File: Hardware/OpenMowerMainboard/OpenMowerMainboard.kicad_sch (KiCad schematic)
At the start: 26 parts

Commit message: Fuse holders and aternative led led pn from lcsc added
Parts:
- D23: LCSC (none) -> C84257
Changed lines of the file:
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@@
+      (effects (font (size 1.27 1.27)) hide)
+    )
+    (property "LCSC" "C84257" (id 7) (at 325.755 201.295 0)
       (effects (font (size 1.27 1.27)) hide)
     )

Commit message: BOM changes
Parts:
- FID1, FID10, FID11, FID12, FID13, FID14, FID15, FID16, FID2, FID3, FID4, FID5, FID6, FID7, FID8, FID9, H1, H2, H3, H4: DNP (none) -> Y
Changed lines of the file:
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@@
+      (effects (font (size 1.27 1.27)) hide)
+    )
+    (property "DNP" "Y" (id 5) (at 373.38 240.03 0)
       (effects (font (size 1.27 1.27)) hide)
     )
@@
       (effects (font (size 1.27 1.27)) hide)
     )
+    (property "DNP" "Y" (id 5) (at 378.46 240.03 0)
+      (effects (font (size 1.27 1.27)) hide)
+    )
     (pin "1")
   )
@@
       (effects (font (size 1.27 1.27)) hide)
     )
+    (property "DNP" "Y" (id 5) (at 383.54 240.03 0)
+      (effects (font (size 1.27 1.27)) hide)
+    )
     (pin "1")
   )
@@
       (effects (font (size 1.27 1.27)) hide)
     )
+    (property "DNP" "Y" (id 5) (at 388.62 240.03 0)
+      (effects (font (size 1.27 1.27)) hide)
+    )
     (pin "1")
   )
@@
       (effects (font (size 1.27 1.27)) hide)
     )
+    (property "DNP" "Y" (id 5) (at 380.365 38.735 0)
+      (effects (font (size 1.27 1.27)) hide)
+    )
   )
   (symbol (lib_id "Mechanical:Fiducial") (at 380.365 52.07 0) (unit 1)
@@
     )
     (property "Config" "do not place" (id 4) (at 380.365 52.07 0)
+      (effects (font (size 1.27 1.27)) hide)
+    )
+    (property "DNP" "Y" (id 5) (at 380.365 52.07 0)
       (effects (font (size 1.27 1.27)) hide)
     )
@@
       (effects (font (size 1.27 1.27)) hide)
     )
+    (property "DNP" "Y" (id 5) (at 380.365 25.4 0)
+      (effects (font (size 1.27 1.27)) hide)
+    )
   )
   (symbol (lib_id "Mechanical:Fiducial") (at 368.3 43.18 0) (unit 1)
@@
       (effects (font (size 1.27 1.27)) hide)
     )
+    (property "DNP" "Y" (id 5) (at 368.3 43.18 0)
+      (effects (font (size 1.27 1.27)) hide)
+    )
   )
   (symbol (lib_id "Mechanical:Fiducial") (at 368.3 47.625 0) (unit 1)
@@
     )
     (property "Config" "do not place" (id 4) (at 368.3 47.625 0)
+      (effects (font (size 1.27 1.27)) hide)
+    )
+    (property "DNP" "Y" (id 5) (at 368.3 47.625 0)
       (effects (font (size 1.27 1.27)) hide)
     )
@@
       (effects (font (size 1.27 1.27)) hide)
     )
+    (property "DNP" "Y" (id 5) (at 380.365 29.845 0)
+      (effects (font (size 1.27 1.27)) hide)
+    )
   )
   (symbol (lib_id "Device:LED") (at 325.755 201.295 90) (unit 1)
@@
     )
     (property "Config" "do not place" (id 4) (at 368.3 25.4 0)
+      (effects (font (size 1.27 1.27)) hide)
+    )
+    (property "DNP" "Y" (id 5) (at 368.3 25.4 0)
       (effects (font (size 1.27 1.27)) hide)
     )
@@
       (effects (font (size 1.27 1.27)) hide)
     )
+    (property "DNP" "Y" (id 5) (at 368.3 56.515 0)
+      (effects (font (size 1.27 1.27)) hide)
+    )
   )
   (symbol (lib_id "power:GND") (at 76.835 88.9 90) (unit 1)
@@
       (effects (font (size 1.27 1.27)) hide)
     )
+    (property "DNP" "Y" (id 5) (at 368.3 38.735 0)
+      (effects (font (size 1.27 1.27)) hide)
+    )
   )
   (symbol (lib_id "Device:R") (at 95.25 156.845 180) (unit 1)
@@
       (effects (font (size 1.27 1.27)) hide)
     )
+    (property "DNP" "Y" (id 5) (at 368.3 52.07 0)
+      (effects (font (size 1.27 1.27)) hide)
+    )
   )
   (symbol (lib_id "power:+5V") (at 325.755 193.04 0) (unit 1)
@@
       (effects (font (size 1.27 1.27)) hide)
     )
+    (property "DNP" "Y" (id 5) (at 380.365 34.29 0)
+      (effects (font (size 1.27 1.27)) hide)
+    )
   )
   (symbol (lib_id "Mechanical:Fiducial") (at 380.365 43.18 0) (unit 1)
@@
       (effects (font (size 1.27 1.27)) hide)
     )
+    (property "DNP" "Y" (id 5) (at 380.365 43.18 0)
+      (effects (font (size 1.27 1.27)) hide)
+    )
   )
   (symbol (lib_id "Mechanical:Fiducial") (at 380.365 47.625 0) (unit 1)
@@
     )
     (property "Config" "do not place" (id 4) (at 380.365 47.625 0)
+      (effects (font (size 1.27 1.27)) hide)
+    )
+    (property "DNP" "Y" (id 5) (at 380.365 47.625 0)
       (effects (font (size 1.27 1.27)) hide)
     )
@@
     )
     (property "Config" "do not place" (id 4) (at 368.3 29.845 0)
+      (effects (font (size 1.27 1.27)) hide)
+    )
+    (property "DNP" "Y" (id 5) (at 368.3 29.845 0)
       (effects (font (size 1.27 1.27)) hide)
     )
@@
       (effects (font (size 1.27 1.27)) hide)
     )
+    (property "DNP" "Y" (id 5) (at 380.365 56.515 0)
+      (effects (font (size 1.27 1.27)) hide)
+    )
   )
   (symbol (lib_id "Device:R") (at 325.755 210.185 180) (unit 1)
@@
     )
     (property "Config" "do not place" (id 4) (at 368.3 34.29 0)
+      (effects (font (size 1.27 1.27)) hide)
+    )
+    (property "DNP" "Y" (id 5) (at 368.3 34.29 0)
       (effects (font (size 1.27 1.27)) hide)
     )
@@
     )
     (path "/ea926745-863d-461e-9df3-dbf32112727b/1dbfe119-2837-4ceb-9076-5a2712ad0b2e"
-      (reference "C9") (unit 1) (value "DNP") (footprint "Capacitor_SMD:CP_Elec_10x12.5")
+      (reference "C9") (unit 1) (value "680uF") (footprint "Capacitor_SMD:CP_Elec_10x12.5")
     )
     (path "/ea926745-863d-461e-9df3-dbf32112727b/28797dd3-5c25-40ea-9029-91b4bdf67bc8"
-      (reference "C10") (unit 1) (value "680uF") (footprint "Capacitor_SMD:CP_Elec_10x12.5")
+      (reference "C10") (unit 1) (value "DNP") (footprint "Capacitor_SMD:CP_Elec_10x12.5")
     )
     (path "/ea926745-863d-461e-9df3-dbf32112727b/254c5ed7-6a5e-462f-bb7e-ae89a4710395"
@@
     )
     (path "/ea926745-863d-461e-9df3-dbf32112727b/5017618a-3028-4818-b382-40d730510d49"
-      (reference "C23") (unit 1) (value "DNP") (footprint "Capacitor_SMD:CP_Elec_10x12.5")
+      (reference "C23") (unit 1) (value "680uF") (footprint "Capacitor_SMD:CP_Elec_10x12.5")
     )
     (path "/c4934db8-1638-4ac4-bd06-84d03b3fc106/2884b602-ea4b-4182-a4ff-ddb6a99ed5db"
@@
       (reference "JP6") (unit 1) (value "SolderJumper_2_Bridged") (footprint "Jumper:SolderJumper-2_P1.3mm_Bridged_RoundedPad1.0x1.5mm")
     )
+    (path "/00000000-0000-0000-0000-000061080954/86e7b903-a105-407a-b12f-ed15cd7fb4ed"
+      (reference "JP7") (unit 1) (value "SolderJumper_2_Bridged") (footprint "Jumper:SolderJumper-2_P1.3mm_Bridged_RoundedPad1.0x1.5mm")
+    )
+    (path "/00000000-0000-0000-0000-000061080954/4ed5a4cb-42d2-4cd1-a2f4-be7f70116c48"
+      (reference "JP8") (unit 1) (value "SolderJumper_2_Bridged") (footprint "Jumper:SolderJumper-2_P1.3mm_Bridged_RoundedPad1.0x1.5mm")
+    )
     (path "/ea926745-863d-461e-9df3-dbf32112727b/37b9c720-0c02-41f5-8880-c0bb97743a0d"
       (reference "L1") (unit 1) (value "4.7uH 5A") (footprint "Inductor_SMD:L_Vishay_IHLP-2525")
@@
     )
     (path "/ea926745-863d-461e-9df3-dbf32112727b/5149161d-2f51-4282-870f-10edba0d6f25"
-      (reference "U1") (unit 1) (value "LM2596S_MODULE") (footprint "MyModules:LM2596S_MODULE")
+      (reference "U1") (unit 1) (value "DNP") (footprint "MyModules:LM2596S_MODULE")
     )
     (path "/989a400d-9ce2-403e-a19e-ad0a758fe27c/6ea01d83-d7f6-4dbf-a272-c95bedd03712"

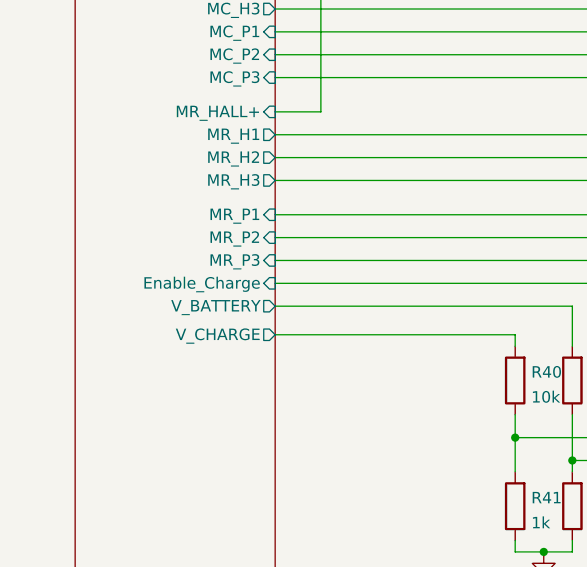
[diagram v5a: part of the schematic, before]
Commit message: fix: fixed ERC/DRC errors, removed LM2596S
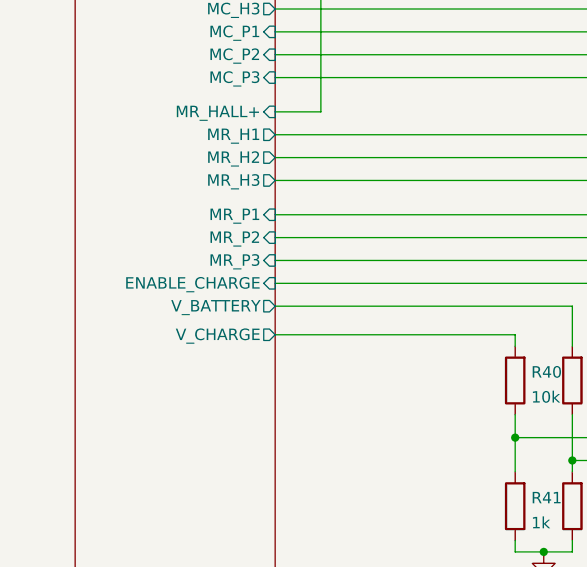
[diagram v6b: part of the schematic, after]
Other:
- sheet RobotConnectors ports: added ENABLE_CHARGE; removed Enable_Charge
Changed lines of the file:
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@@
       (effects (font (size 1.27 1.27)) (justify right))
     )
-    (pin "Enable_Charge" input (at 68.58 132.08 0)
+    (pin "ENABLE_CHARGE" input (at 68.58 132.08 0)
       (effects (font (size 1.27 1.27)) (justify right))
     )
@@
   )
   (symbol_instances
+    (path "/ea926745-863d-461e-9df3-dbf32112727b/bca34ef9-4aab-4ab9-889d-1e8c0af877f1"
+      (reference "#FLG0101") (unit 1) (value "PWR_FLAG") (footprint "")
+    )
+    (path "/ea926745-863d-461e-9df3-dbf32112727b/3935cc4c-fd83-4144-a6f3-151fe6ee58c5"
+      (reference "#FLG0102") (unit 1) (value "PWR_FLAG") (footprint "")
+    )
     (path "/00000000-0000-0000-0000-000061040c60/00000000-0000-0000-0000-00006105dd51"
       (reference "#PWR0101") (unit 1) (value "GND") (footprint "")
@@
       (reference "#PWR0105") (unit 1) (value "GND") (footprint "")
     )
-    (path "/ea926745-863d-461e-9df3-dbf32112727b/b8cb89b3-4805-4e56-9325-1f9afe8522c4"
-      (reference "#PWR0106") (unit 1) (value "GND") (footprint "")
-    )
-    (path "/ea926745-863d-461e-9df3-dbf32112727b/ac238d30-44a0-44b9-b5c5-a58e54e3f16e"
-      (reference "#PWR0107") (unit 1) (value "+5V") (footprint "")
-    )
     (path "/00000000-0000-0000-0000-000061040c60/3e1c4d9d-6fcf-4de0-994d-a29d1c10cdf1"
       (reference "#PWR0108") (unit 1) (value "GND") (footprint "")
@@
       (reference "TP5") (unit 1) (value "TestPoint") (footprint "TestPoint:TestPoint_Pad_D2.0mm")
     )
-    (path "/ea926745-863d-461e-9df3-dbf32112727b/5149161d-2f51-4282-870f-10edba0d6f25"
-      (reference "U1") (unit 1) (value "DNP") (footprint "MyModules:LM2596S_MODULE")
-    )
     (path "/989a400d-9ce2-403e-a19e-ad0a758fe27c/6ea01d83-d7f6-4dbf-a272-c95bedd03712"

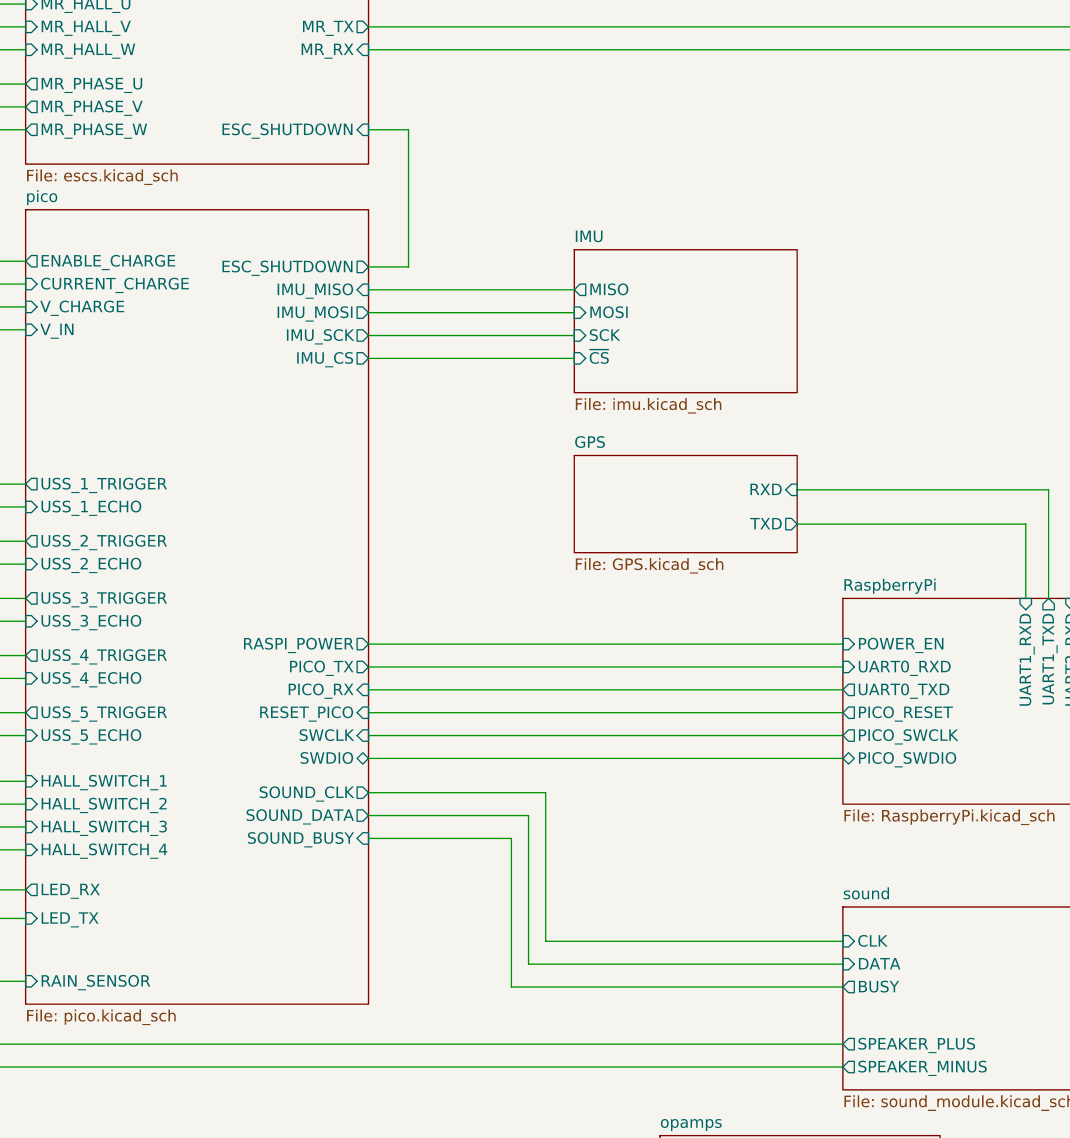
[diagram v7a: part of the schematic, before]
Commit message: fix(imu): update and reroute sound/imu connections
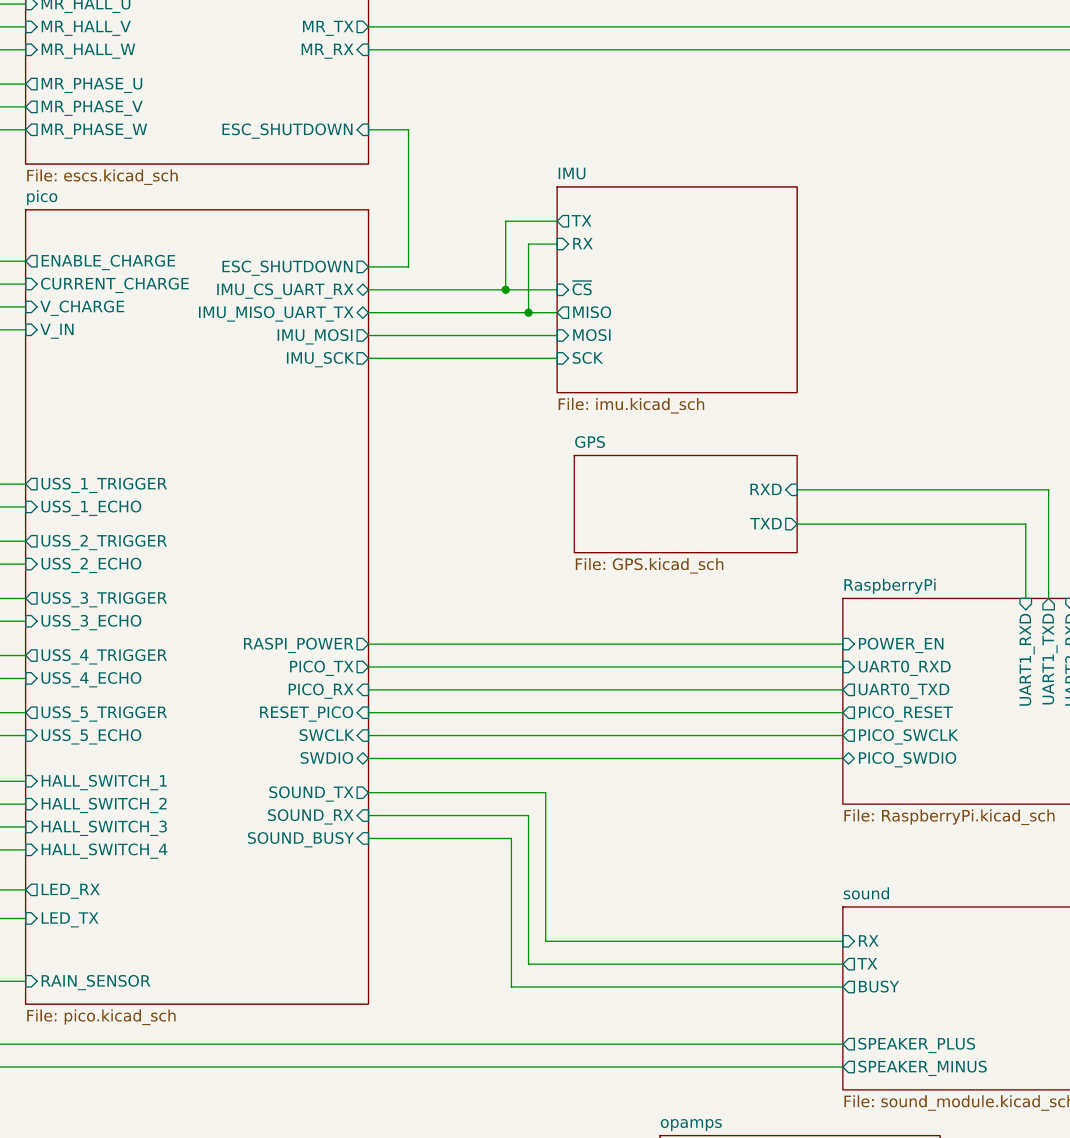
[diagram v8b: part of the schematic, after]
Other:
- sheet IMU ports: added RX, TX; removed none
- sheet pico ports: added IMU_CS_UART_RX, IMU_MISO_UART_TX, SOUND_RX, SOUND_TX; removed IMU_CS, IMU_MISO, SOUND_CLK, SOUND_DATA
- sheet sound ports: added RX, TX; removed CLK, DATA
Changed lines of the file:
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@@
 (kicad_sch (version 20211123) (generator eeschema)
   (paper "A3")
+  (junction (at 186.055 147.32) (diameter 0) (color 0 0 0 0)
+  )
   (junction (at 73.66 93.98) (diameter 0) (color 0 0 0 0)
   )
@@
   (junction (at 73.66 67.31) (diameter 0) (color 0 0 0 0)
   )
+  (junction (at 188.595 149.86) (diameter 0) (color 0 0 0 0)
+  )
   (wire (pts (xy 218.44 169.545) (xy 246.38 169.545))
     (stroke (width 0) (type default) (color 0 0 0 0))
@@
     (stroke (width 0) (type default) (color 0 0 0 0))
   )
-  (wire (pts (xy 170.815 152.4) (xy 193.675 152.4))
-    (stroke (width 0) (type default) (color 0 0 0 0))
-  )
   (wire (pts (xy 378.46 242.57) (xy 378.46 245.11))
     (stroke (width 0) (type default) (color 0 0 0 0))
@@
     (stroke (width 0) (type default) (color 0 0 0 0))
   )
-  (wire (pts (xy 170.815 154.94) (xy 193.675 154.94))
+  (wire (pts (xy 188.595 149.86) (xy 191.77 149.86))
+    (stroke (width 0) (type default) (color 0 0 0 0))
+  )
+  (wire (pts (xy 188.595 149.86) (xy 188.595 142.24))
     (stroke (width 0) (type default) (color 0 0 0 0))
   )
@@
     (stroke (width 0) (type default) (color 0 0 0 0))
   )
+  (wire (pts (xy 170.815 147.32) (xy 186.055 147.32))
+    (stroke (width 0) (type default) (color 0 0 0 0))
+  )
   (wire (pts (xy 101.6 151.765) (xy 132.715 151.765))
     (stroke (width 0) (type default) (color 0 0 0 0))
@@
     (stroke (width 0) (type default) (color 0 0 0 0))
   )
-  (wire (pts (xy 170.815 149.86) (xy 193.675 149.86))
-    (stroke (width 0) (type default) (color 0 0 0 0))
-  )
   (wire (pts (xy 383.54 245.11) (xy 388.62 245.11))
     (stroke (width 0) (type default) (color 0 0 0 0))
@@
     (stroke (width 0) (type default) (color 0 0 0 0))
   )
+  (wire (pts (xy 170.815 149.86) (xy 188.595 149.86))
+    (stroke (width 0) (type default) (color 0 0 0 0))
+  )
+  (wire (pts (xy 186.055 139.7) (xy 191.77 139.7))
+    (stroke (width 0) (type default) (color 0 0 0 0))
+  )
   (wire (pts (xy 95.25 146.685) (xy 95.25 149.225))
     (stroke (width 0) (type default) (color 0 0 0 0))
@@
     (stroke (width 0) (type default) (color 0 0 0 0))
   )
+  (wire (pts (xy 186.055 147.32) (xy 186.055 139.7))
+    (stroke (width 0) (type default) (color 0 0 0 0))
+  )
   (wire (pts (xy 170.815 191.77) (xy 223.52 191.77))
     (stroke (width 0) (type default) (color 0 0 0 0))
@@
     (stroke (width 0) (type default) (color 0 0 0 0))
   )
-  (wire (pts (xy 170.815 147.32) (xy 193.675 147.32))
-    (stroke (width 0) (type default) (color 0 0 0 0))
-  )
   (wire (pts (xy 68.58 88.9) (xy 76.835 88.9))
     (stroke (width 0) (type default) (color 0 0 0 0))
@@
     (stroke (width 0) (type default) (color 0 0 0 0))
   )
+  (wire (pts (xy 170.815 154.94) (xy 191.77 154.94))
+    (stroke (width 0) (type default) (color 0 0 0 0))
+  )
   (wire (pts (xy 388.62 245.11) (xy 388.62 242.57))
     (stroke (width 0) (type default) (color 0 0 0 0))
@@
     (stroke (width 0) (type default) (color 0 0 0 0))
   )
+  (wire (pts (xy 170.815 152.4) (xy 191.77 152.4))
+    (stroke (width 0) (type default) (color 0 0 0 0))
+  )
   (wire (pts (xy 123.19 144.145) (xy 123.19 132.08))
     (stroke (width 0) (type default) (color 0 0 0 0))
   )
+  (wire (pts (xy 188.595 142.24) (xy 191.77 142.24))
+    (stroke (width 0) (type default) (color 0 0 0 0))
+  )
   (wire (pts (xy 68.58 69.85) (xy 132.715 69.85))
     (stroke (width 0) (type default) (color 0 0 0 0))
@@
   )
   (wire (pts (xy 68.58 124.46) (xy 132.715 124.46))
+    (stroke (width 0) (type default) (color 0 0 0 0))
+  )
+  (wire (pts (xy 186.055 147.32) (xy 191.77 147.32))
     (stroke (width 0) (type default) (color 0 0 0 0))
   )
@@
       (effects (font (size 1.27 1.27)) (justify left))
     )
-    (pin "DATA" input (at 223.52 222.25 180)
-      (effects (font (size 1.27 1.27)) (justify left))
-    )
-    (pin "CLK" input (at 223.52 219.71 180)
+    (pin "TX" output (at 223.52 222.25 180)
+      (effects (font (size 1.27 1.27)) (justify left))
+    )
+    (pin "RX" input (at 223.52 219.71 180)
       (effects (font (size 1.27 1.27)) (justify left))
     )
@@
       (effects (font (size 1.27 1.27)) (justify right))
     )
-    (pin "SOUND_CLK" output (at 170.815 203.2 0)
-      (effects (font (size 1.27 1.27)) (justify right))
-    )
-    (pin "SOUND_DATA" output (at 170.815 205.74 0)
+    (pin "SOUND_TX" output (at 170.815 203.2 0)
+      (effects (font (size 1.27 1.27)) (justify right))
+    )
+    (pin "SOUND_RX" input (at 170.815 205.74 0)
       (effects (font (size 1.27 1.27)) (justify right))
     )
@@
       (effects (font (size 1.27 1.27)) (justify left))
     )
-    (pin "IMU_MISO" input (at 170.815 147.32 0)
-      (effects (font (size 1.27 1.27)) (justify right))
-    )
-    (pin "IMU_SCK" output (at 170.815 152.4 0)
-      (effects (font (size 1.27 1.27)) (justify right))
-    )
-    (pin "IMU_CS" output (at 170.815 154.94 0)
-      (effects (font (size 1.27 1.27)) (justify right))
-    )
-    (pin "IMU_MOSI" output (at 170.815 149.86 0)
+    (pin "IMU_MISO_UART_TX" bidirectional (at 170.815 149.86 0)
+      (effects (font (size 1.27 1.27)) (justify right))
+    )
+    (pin "IMU_SCK" output (at 170.815 154.94 0)
+      (effects (font (size 1.27 1.27)) (justify right))
+    )
+    (pin "IMU_CS_UART_RX" bidirectional (at 170.815 147.32 0)
+      (effects (font (size 1.27 1.27)) (justify right))
+    )
+    (pin "IMU_MOSI" output (at 170.815 152.4 0)
       (effects (font (size 1.27 1.27)) (justify right))
     )
@@
     )
   )
-  (sheet (at 193.675 142.875) (size 24.765 15.875) (fields_autoplaced)
+  (sheet (at 191.77 135.89) (size 26.67 22.86) (fields_autoplaced)
     (stroke (width 0.1524) (type solid) (color 0 0 0 0))
     (fill (color 0 0 0 0.0000))
-    (property "Sheet name" "IMU" (id 0) (at 193.675 142.1634 0)
+    (property "Sheet name" "IMU" (id 0) (at 191.77 135.1784 0)
       (effects (font (size 1.27 1.27)) (justify left bottom))
     )
-    (property "Sheet file" "imu.kicad_sch" (id 1) (at 193.675 159.3346 0)
+    (property "Sheet file" "imu.kicad_sch" (id 1) (at 191.77 159.3346 0)
       (effects (font (size 1.27 1.27)) (justify left top))
     )
-    (pin "SCK" input (at 193.675 152.4 180)
-      (effects (font (size 1.27 1.27)) (justify left))
-    )
-    (pin "MISO" output (at 193.675 147.32 180)
-      (effects (font (size 1.27 1.27)) (justify left))
-    )
-    (pin "MOSI" input (at 193.675 149.86 180)
-      (effects (font (size 1.27 1.27)) (justify left))
-    )
-    (pin "~{CS}" input (at 193.675 154.94 180)
-      (effects (font (size 1.27 1.27)) (justify left))
-    )
+    (pin "SCK" input (at 191.77 154.94 180)
+      (effects (font (size 1.27 1.27)) (justify left))
+    )
+    (pin "MISO" output (at 191.77 149.86 180)
+      (effects (font (size 1.27 1.27)) (justify left))
+    )
+    (pin "MOSI" input (at 191.77 152.4 180)
+      (effects (font (size 1.27 1.27)) (justify left))
+    )
+    (pin "~{CS}" input (at 191.77 147.32 180)
+      (effects (font (size 1.27 1.27)) (justify left))
+    )
+    (pin "RX" input (at 191.77 142.24 180)
+      (effects (font (size 1.27 1.27)) (justify left))
+    )
+    (pin "TX" output (at 191.77 139.7 180)
+      (effects (font (size 1.27 1.27)) (justify left))
+    )
